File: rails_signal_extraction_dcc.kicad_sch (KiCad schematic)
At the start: 1 part

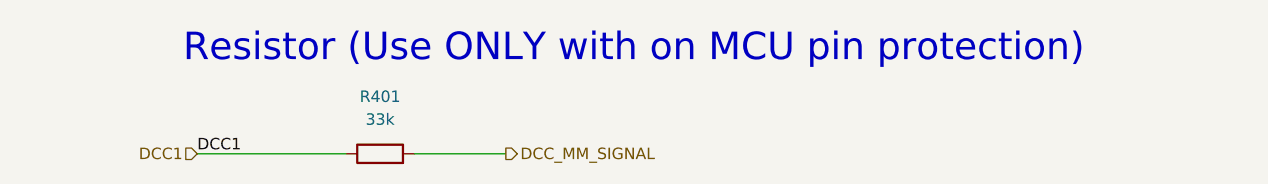
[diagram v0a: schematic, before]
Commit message: Fix - Remove ERC error, refresh annotation
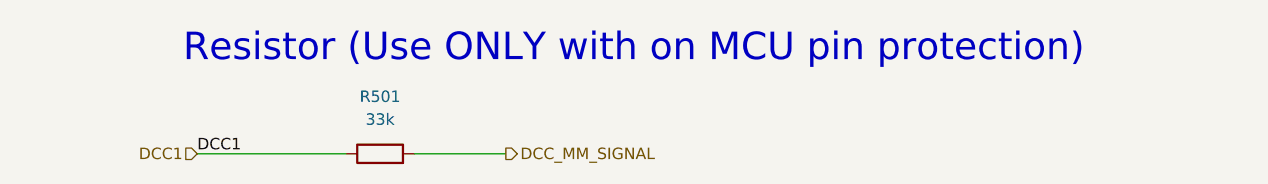
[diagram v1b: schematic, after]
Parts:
- renumbered R401 to R501
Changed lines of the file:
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@@
 		(dnp no)
 		(fields_autoplaced yes)
-		(property "Reference" "R401"
+		(property "Reference" "R501"
 			(at 52.07 31.75 90)
 			(effects
@@
 			(project "xDuinoRails-Fortuna-M"
 				(path "/fb33ec4e-6596-45d2-a121-8d3475acd69a/c9229de7-1ed3-435d-9b11-33fa2e05ec65/3f6df3ac-cacb-4a62-a6cd-afb105728627"
-					(reference "R401")
+					(reference "R501")
 					(unit 1)
 				)

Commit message: Fix - revert to working model
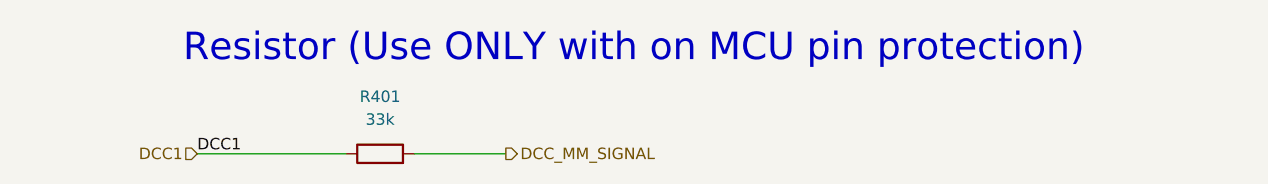
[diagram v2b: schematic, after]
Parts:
- renumbered R501 to R401
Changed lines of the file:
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@@
 		(dnp no)
 		(fields_autoplaced yes)
-		(property "Reference" "R501"
+		(property "Reference" "R401"
 			(at 52.07 31.75 90)
 			(effects
@@
 			(project "xDuinoRails-Fortuna-M"
 				(path "/fb33ec4e-6596-45d2-a121-8d3475acd69a/c9229de7-1ed3-435d-9b11-33fa2e05ec65/3f6df3ac-cacb-4a62-a6cd-afb105728627"
-					(reference "R501")
+					(reference "R401")
 					(unit 1)
 				)
